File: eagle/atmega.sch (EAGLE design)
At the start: 67 parts, among them IC1 TO 5V, IC2 LM339D, Q2 16MHz, U1 ATMEGA328P-AU, X2 MINI-USB_SHIELD5P4-32005-501

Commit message: Podłączenie USB, Początek podłączania do sterownika.
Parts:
- added C10: 1uF, capacitor-wima:C2,5-3
- added R1, R22: 22R, resistor:R-EU_M0805
- R10, R12, R13, R14, R15, R16, R17, R18, R2, R20, R21, R3, R4, R5, R6, R7, R8, R9: device rcl:R-EU_R0805 -> resistor:R-EU_M0805
- ZWORKA: device rcl:R-EU_0613/5V -> rcl:R-EU_0204/5
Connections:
- removed net N$14: U$6.(PCINT5/OC1A/OC4B/ADC12)PB5
- removed net N$15: U$6.(PCINT6/OC1B/OC4B/ADC13)PB6
- removed net N$17: U$6.(OC3A/OC4A)PC6
- removed net N$18: U$6.(ICP3/CLK0/OC4A)PC7
- removed net N$27: U$6.(ICP1/ADC8)PD4
- removed net N$34: U$6.(T1/OC4D/ADC9)PD6
- removed net N$35: U$6.(T0/OC4D/ADC10)PD7
- removed net N$45: U$6.VBUS
- removed net N$46: U$6.UCAP
- removed net N$47: U$6.UGND
- removed net N$58: U$6.GND
- removed net N$60: U$6.VCC
- removed net N$64: X2G$1.2
- removed net N$66: X2G$1.4
- removed net N$67: X2G$1.5
- new net N$49: R1.2, X2G$1.2
- new net UCAP: C10.2, U$6.UCAP
- new net UGND: C10.1, U$6.UGND, X2G$1.5
- new net VBUS: U$6.VBUS, X2G$1.4
- net AIN1: now also U$6.(T1/OC4D/ADC9)PD6
- net AIN2: now also U$6.(ICP1/ADC8)PD4
- net BIN1: now also U$6.(PCINT6/OC1B/OC4B/ADC13)PB6
- net BIN2: now also U$6.(OC3A/OC4A)PC6
- net D+: now also R22.1
- net D-: now also R1.1
- net GND: now also U$6.GND
- net N$65: now also R22.2
- net PWMA: now also U$6.(T0/OC4D/ADC10)PD7
- net PWMB: now also U$6.(ICP3/CLK0/OC4A)PC7
- net STBY: now also U$6.(PCINT5/OC1A/OC4B/ADC12)PB5
- net VCC: now also U$6.VCC, U1.VCC_2

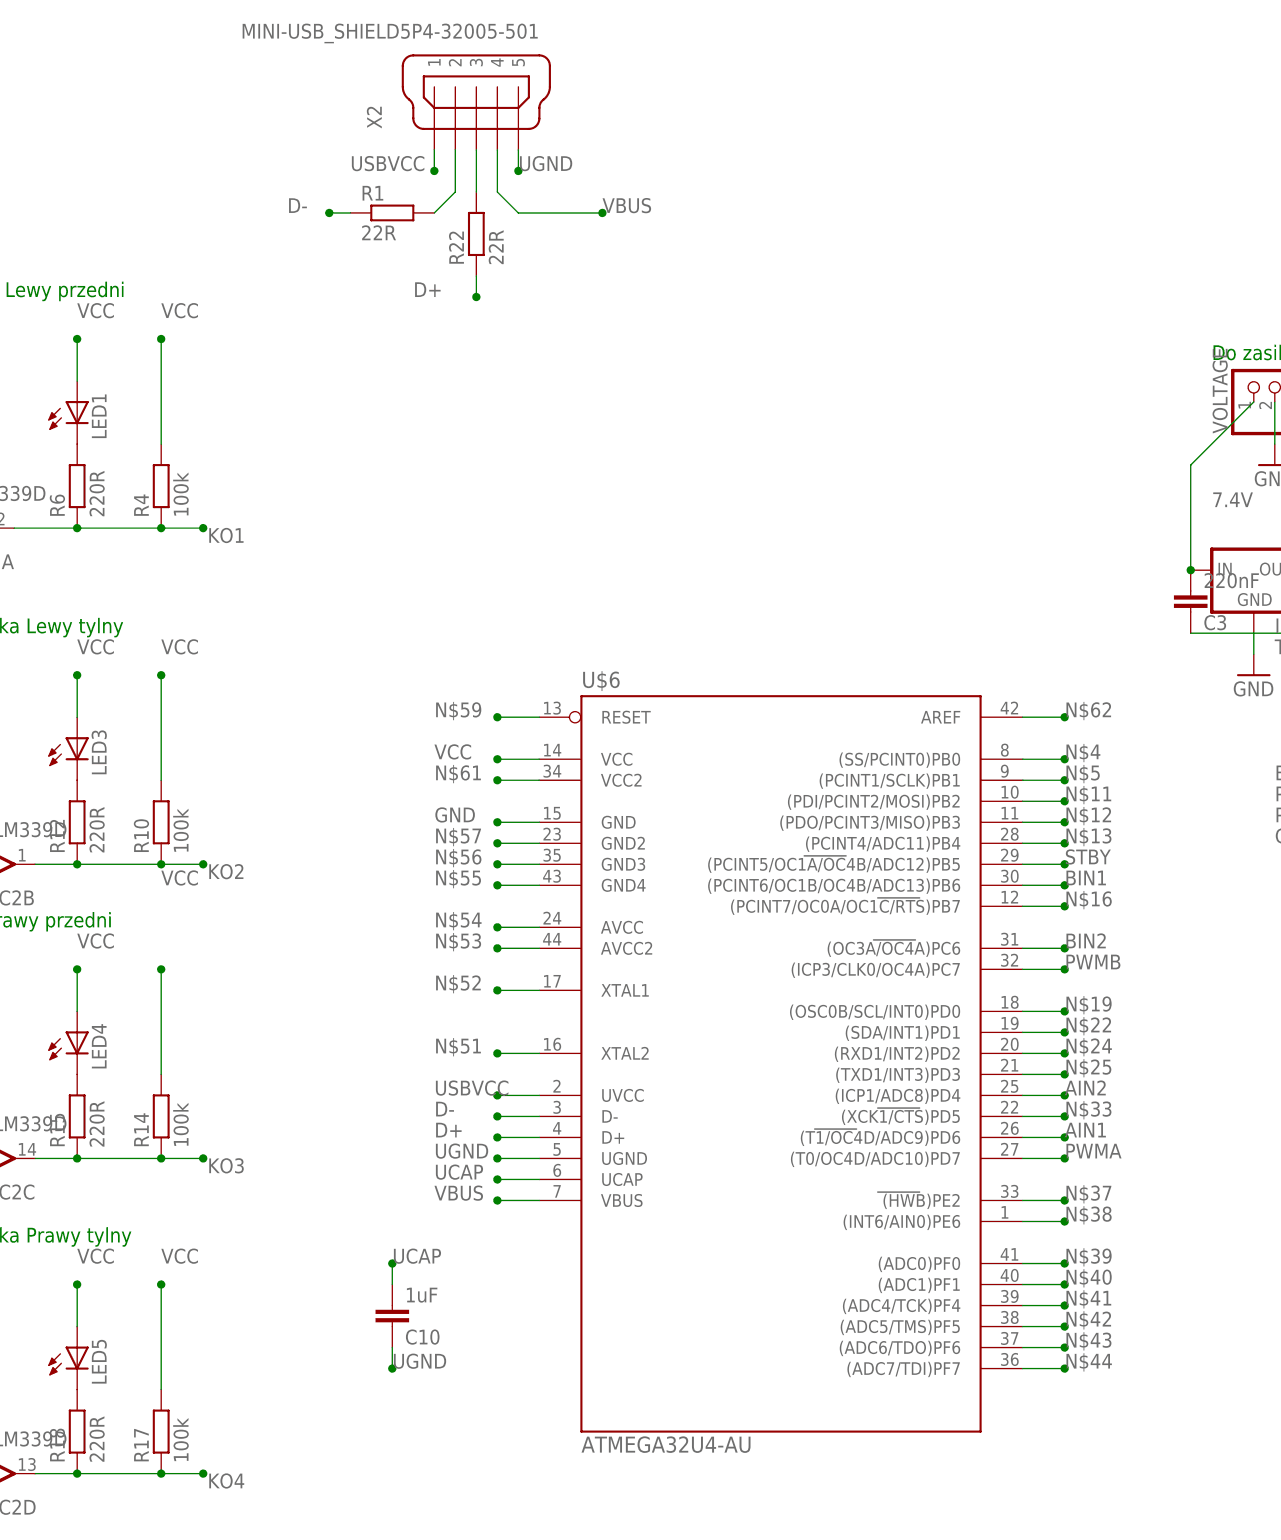
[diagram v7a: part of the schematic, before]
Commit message: Usunąłem ATmega32U
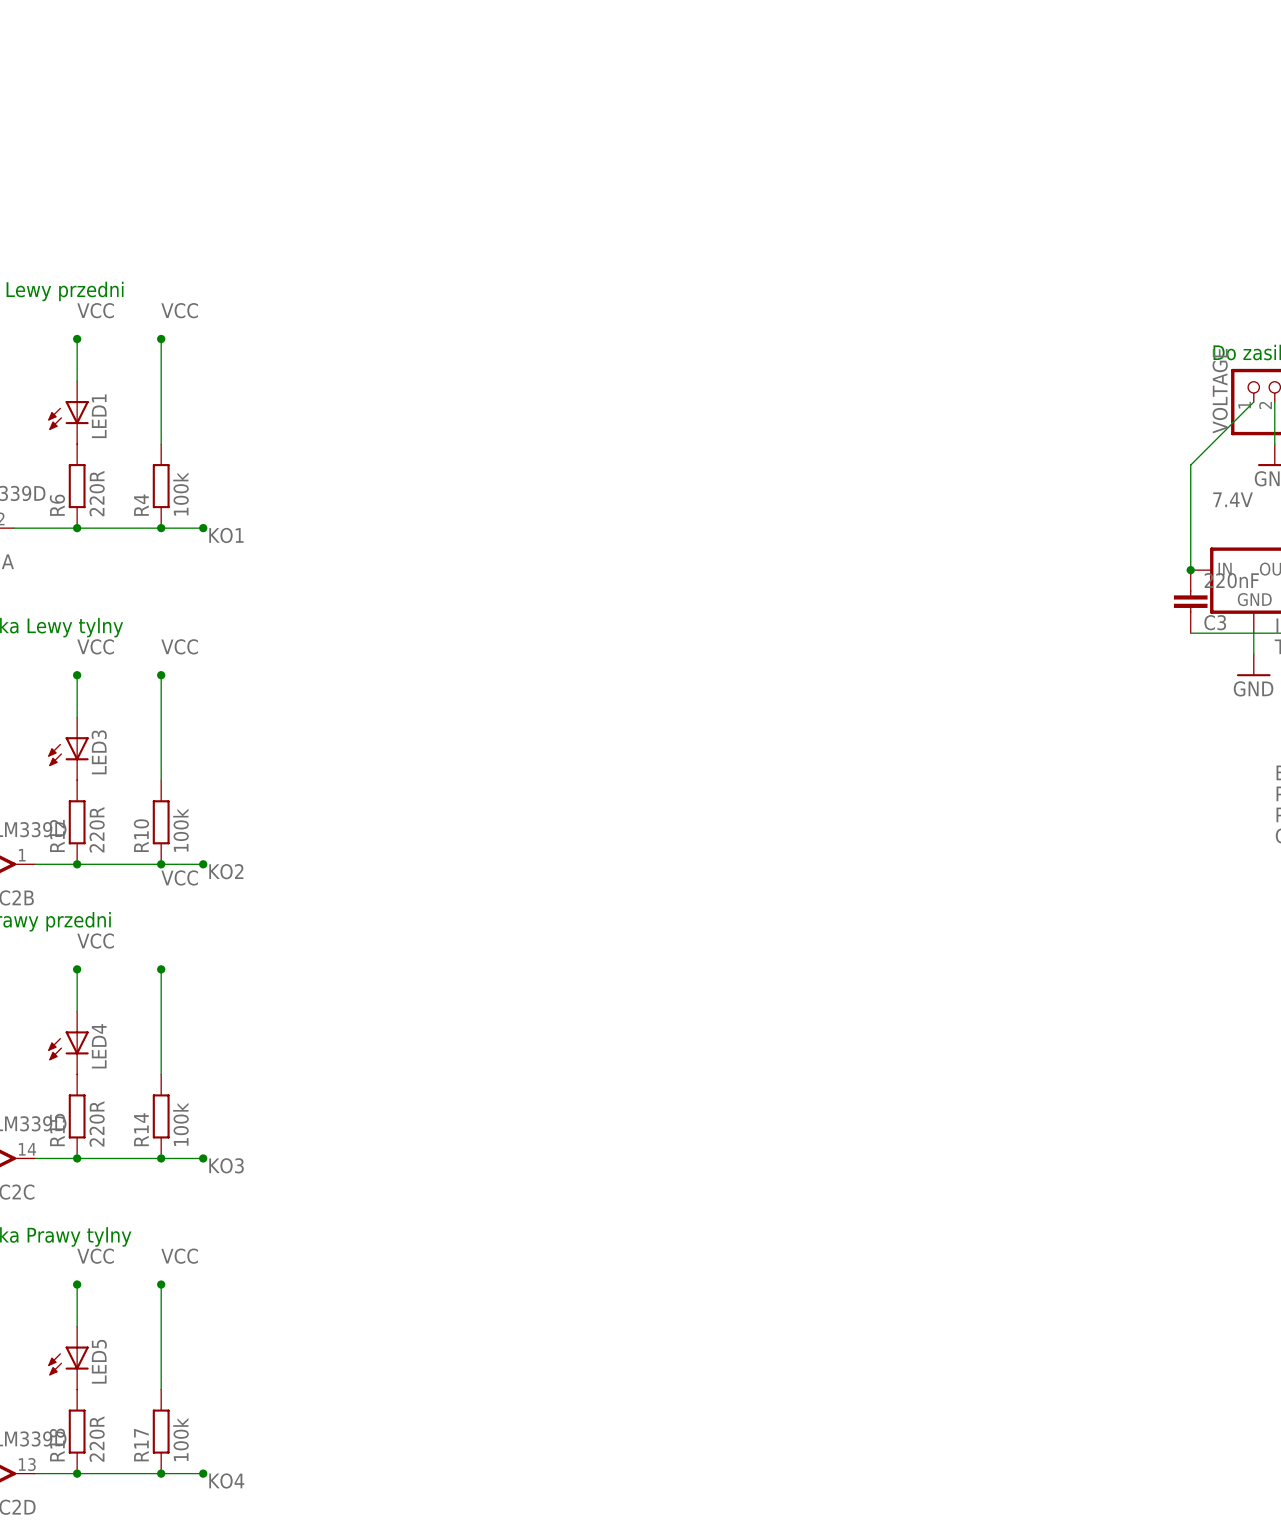
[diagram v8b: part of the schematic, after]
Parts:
- removed C10: 1uF, capacitor-wima:C2,5-3
- removed R1, R22: 22R, resistor:R-EU_M0805
- removed U$6: ATMEGA32U4-AU, mega32U4:ATMEGA32U4-AU
- removed X2: MINI-USB_SHIELD5P4-32005-501, con-cypressindustries:MINI-USB_SHIELD5P4-32005-501
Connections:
- removed net D+: R22.1, U$6.D+
- removed net D-: R1.1, U$6.D-
- removed net N$11: U$6.(PDI/PCINT2/MOSI)PB2
- removed net N$12: U$6.(PDO/PCINT3/MISO)PB3
- removed net N$13: U$6.(PCINT4/ADC11)PB4
- removed net N$16: U$6.(PCINT7/OC0A/OC1C/RTS)PB7
- removed net N$19: U$6.(OSC0B/SCL/INT0)PD0
- removed net N$22: U$6.(SDA/INT1)PD1
- removed net N$24: U$6.(RXD1/INT2)PD2
- removed net N$25: U$6.(TXD1/INT3)PD3
- removed net N$33: U$6.(XCK1/CTS)PD5
- removed net N$37: U$6.(HWB)PE2
- removed net N$38: U$6.(INT6/AIN0)PE6
- removed net N$39: U$6.(ADC0)PF0
- removed net N$4: U$6.(SS/PCINT0)PB0
- removed net N$40: U$6.(ADC1)PF1
- removed net N$41: U$6.(ADC4/TCK)PF4
- removed net N$42: U$6.(ADC5/TMS)PF5
- removed net N$43: U$6.(ADC6/TDO)PF6
- removed net N$44: U$6.(ADC7/TDI)PF7
- removed net N$49: R1.2, X2G$1.2
- removed net N$5: U$6.(PCINT1/SCLK)PB1
- removed net N$51: U$6.XTAL2
- removed net N$52: U$6.XTAL1
- removed net N$53: U$6.AVCC2
- removed net N$54: U$6.AVCC
- removed net N$55: U$6.GND4
- removed net N$56: U$6.GND3
- removed net N$57: U$6.GND2
- removed net N$59: U$6.RESET
- removed net N$61: U$6.VCC2
- removed net N$62: U$6.AREF
- removed net N$65: R22.2, X2G$1.3
- removed net UCAP: C10.2, U$6.UCAP
- removed net UGND: C10.1, U$6.UGND, X2G$1.5
- removed net USBVCC: U$6.UVCC, X2G$1.1
- removed net VBUS: U$6.VBUS, X2G$1.4
- net AIN1: no longer U$6.(T1/OC4D/ADC9)PD6
- net AIN2: no longer U$6.(ICP1/ADC8)PD4
- net BIN1: no longer U$6.(PCINT6/OC1B/OC4B/ADC13)PB6
- net BIN2: no longer U$6.(OC3A/OC4A)PC6
- net GND: no longer U$6.GND
- net PWMA: no longer U$6.(T0/OC4D/ADC10)PD7
- net PWMB: no longer U$6.(ICP3/CLK0/OC4A)PC7
- net STBY: no longer U$6.(PCINT5/OC1A/OC4B/ADC12)PB5
- net VCC: no longer U$6.VCC
